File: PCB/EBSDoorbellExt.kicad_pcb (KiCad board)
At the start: 2 copper layers, 65.8 x 49 mm, 273 parts, among them P1 AC in, P2 Doorbell, Q1 BC846C, SW1 Power, SW2 FSM2JSMAA, U1 LM7809CT, U2 LM555N, U3 LTV-817

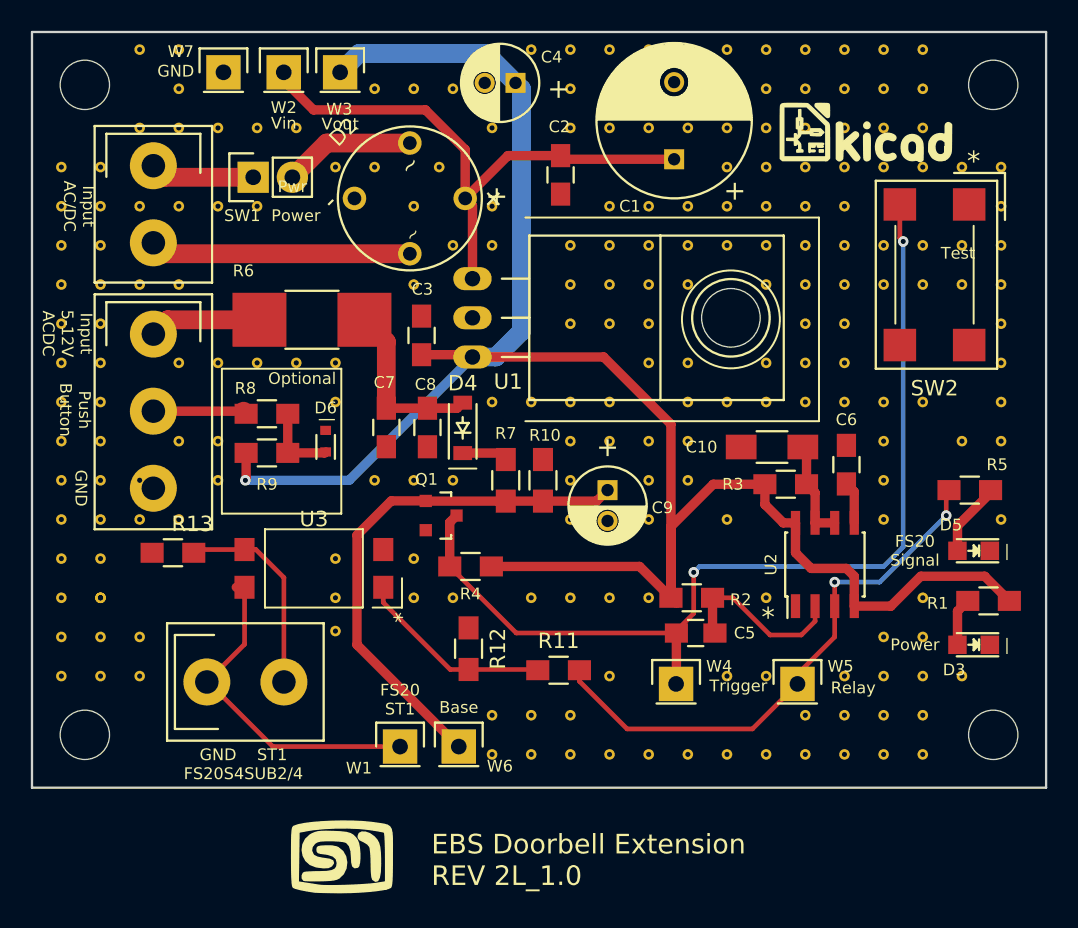
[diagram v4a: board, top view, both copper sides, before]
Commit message: Added protection diode on ground for voltage sensing
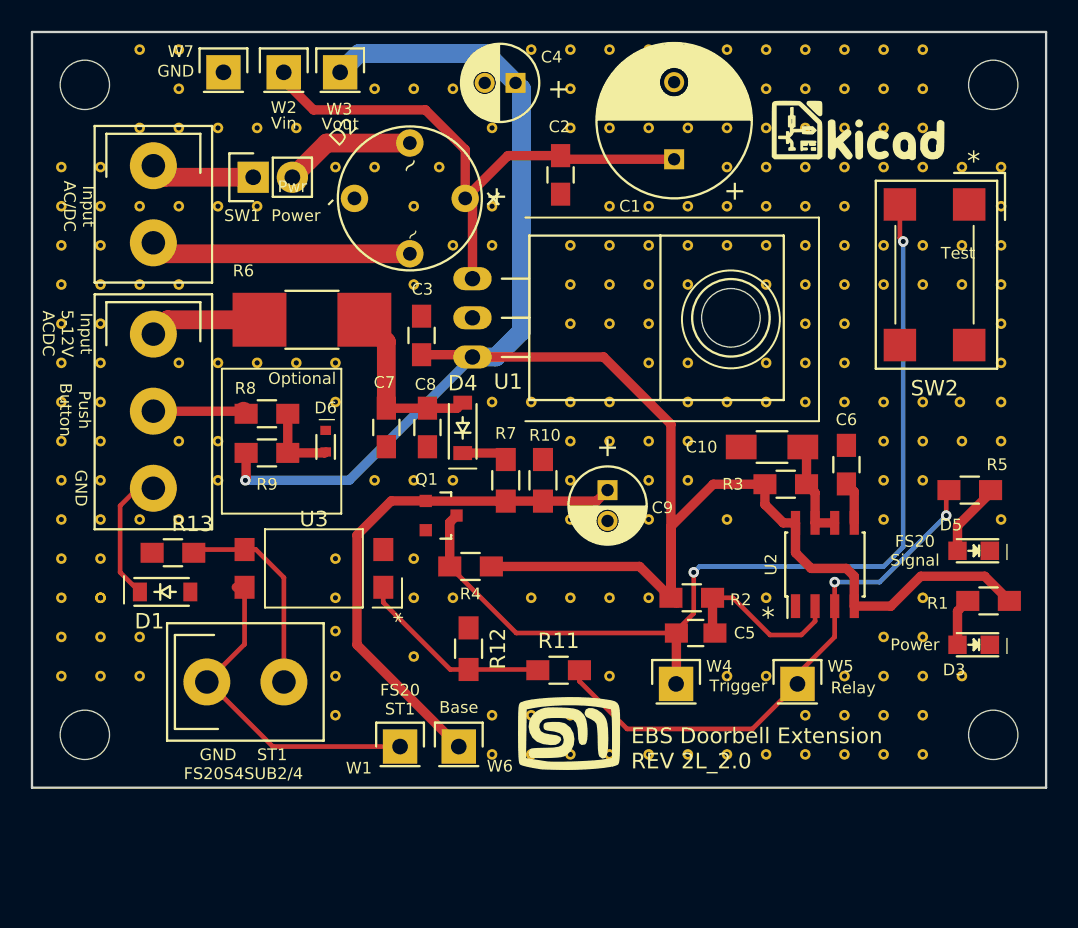
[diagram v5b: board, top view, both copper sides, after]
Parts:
- removed ST**312: Stitch_VIA, EBSDoorbellExt-Footprints:Stitch_VIA
- added D1: 1N4148W, Diodes_SMD:SOD-123, F.Cu at (138.8, 103.8)
- added ST**21712: Stitch_VIA, EBSDoorbellExt-Footprints:Stitch_VIA, F.Cu at (149.9, 111.8)
- added ST**21712: Stitch_VIA, EBSDoorbellExt-Footprints:Stitch_VIA, F.Cu at (154.9, 108.0)
- added ST**21712: Stitch_VIA, EBSDoorbellExt-Footprints:Stitch_VIA, F.Cu at (149.9, 109.2)
- added ST**2310: Stitch_VIA, EBSDoorbellExt-Footprints:Stitch_VIA, F.Cu at (190.4, 91.4)
- added ST**2310: Stitch_VIA, EBSDoorbellExt-Footprints:Stitch_VIA, F.Cu at (188.0, 96.5)
- added ST**2310: Stitch_VIA, EBSDoorbellExt-Footprints:Stitch_VIA, F.Cu at (188.0, 94.0)
- D2: footprint EBSDoorbellExt-Footprints:B80C1500G -> B80C1500G
- moved G*** 16.8 mm to (165.0, 112.9)
- moved G*** 0.52 mm to (183.8, 73.8)
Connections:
- P2 pad 3: GND -> Net-(D1-Pad1)
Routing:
- net Net-(D1-Pad1): track 0.00 -> 8.76 mm
- net Net-(C1-Pad1): track 37.5 -> 38.2 mm
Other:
- board text added: "EBS Doorbell Extension REV 2L_2.0"
- board text removed: "EBS Doorbell Extension REV 2L_1.0"

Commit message: Rev 2 gerbers and stensil order
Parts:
- removed ST**197: Stitch_VIA, EBSDoorbellExt-Footprints:Stitch_VIA
- added ST**21711: Stitch_VIA, EBSDoorbellExt-Footprints:Stitch_VIA, F.Cu at (142.2, 104.1)
- added ST**21711: Stitch_VIA, EBSDoorbellExt-Footprints:Stitch_VIA, F.Cu at (147.3, 104.1)
- added ST**21711: Stitch_VIA, EBSDoorbellExt-Footprints:Stitch_VIA, F.Cu at (147.3, 101.6)
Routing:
- net Net-(MOD1-Pad1): track 22.0 -> 21.4 mm
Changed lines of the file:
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@@
-(kicad_pcb (version 4) (host pcbnew 4.0.2-4+6225~38~ubuntu14.04.1-stable)
+(kicad_pcb (version 4) (host pcbnew 4.0.0-2.201512072331+6194~38~ubuntu14.04.1-stable)
   (general
-    (links 300)
+    (links 302)
     (no_connects 0)
     (area 126.257957 63.6926 199.878044 118.7834)
     (thickness 1.6)
     (drawings 38)
-    (tracks 157)
+    (tracks 156)
     (zones 0)
-    (modules 279)
+    (modules 281)
     (nets 26)
   )
@@
   )
   (setup
-    (last_trace_width 0.6096)
+    (last_trace_width 0.1524)
     (user_trace_width 0.3048)
     (user_trace_width 0.6096)
@@
     (add_net "Net-(SW2-Pad4)")
   )
+  (module EBSDoorbellExt-Footprints:Stitch_VIA (layer F.Cu)
+    (at 142.24 104.14)
+    (zone_connect 2)
+    (fp_text reference ST**21711 (at 0 3.556) (layer F.SilkS) hide
+      (effects (font (size 1 1) (thickness 0.15)))
+    )
+    (fp_text value Stitch_VIA (at 0 -3.81) (layer F.Fab) hide
+      (effects (font (size 1 1) (thickness 0.15)))
+    )
+    (pad 1 thru_hole circle (at 0 0) (size 0.6858 0.6858) (drill 0.3302) (layers *.Cu)
+      (net 2 GND) (zone_connect 2))
+  )
+  (module EBSDoorbellExt-Footprints:Stitch_VIA (layer F.Cu)
+    (at 147.32 104.14)
+    (zone_connect 2)
+    (fp_text reference ST**21711 (at 0 3.556) (layer F.SilkS) hide
+      (effects (font (size 1 1) (thickness 0.15)))
+    )
+    (fp_text value Stitch_VIA (at 0 -3.81) (layer F.Fab) hide
+      (effects (font (size 1 1) (thickness 0.15)))
+    )
+    (pad 1 thru_hole circle (at 0 0) (size 0.6858 0.6858) (drill 0.3302) (layers *.Cu)
+      (net 2 GND) (zone_connect 2))
+  )
+  (module EBSDoorbellExt-Footprints:Stitch_VIA (layer F.Cu)
+    (at 147.32 101.6)
+    (zone_connect 2)
+    (fp_text reference ST**21711 (at 0 3.556) (layer F.SilkS) hide
+      (effects (font (size 1 1) (thickness 0.15)))
+    )
+    (fp_text value Stitch_VIA (at 0 -3.81) (layer F.Fab) hide
+      (effects (font (size 1 1) (thickness 0.15)))
+    )
+    (pad 1 thru_hole circle (at 0 0) (size 0.6858 0.6858) (drill 0.3302) (layers *.Cu)
+      (net 2 GND) (zone_connect 2))
+  )
   (module B80C1500G (layer F.Cu)
     (at 154.686 78.232 225)
@@
   )
   (module EBSDoorbellExt-Footprints:Stitch_VIA (layer F.Cu)
-    (at 177.8 83.82)
-    (zone_connect 2)
-    (fp_text reference ST**197 (at 0 3.556) (layer F.SilkS) hide
-      (effects (font (size 1 1) (thickness 0.15)))
-    )
-    (fp_text value Stitch_VIA (at 0 -3.81) (layer F.Fab) hide
-      (effects (font (size 1 1) (thickness 0.15)))
-    )
-    (pad 1 thru_hole circle (at 0 0) (size 0.6858 0.6858) (drill 0.3302) (layers *.Cu)
-      (net 2 GND) (zone_connect 2))
-  )
-  (module EBSDoorbellExt-Footprints:Stitch_VIA (layer F.Cu)
     (at 172.72 83.82)
     (zone_connect 2)
@@
   (module EBSDoorbellExt-Footprints:LTV_817 (layer F.Cu)
     (at 148.463 102.235 90)
-    (fp_text reference U3 (at 3.2004 0 180) (layer F.SilkS)
+    (fp_text reference U3 (at -3.429 2.286 180) (layer F.SilkS)
       (effects (font (size 1 1) (thickness 0.15)))
     )
@@
     (effects (font (thickness 0.254)))
   )
-  (gr_text | (at 149.225 92.583 90) (layer F.SilkS)
+  (gr_text | (at 149.098 95.504 90) (layer F.SilkS)
     (effects (font (size 0.762 0.762) (thickness 0.1905)))
   )
@@
     (effects (font (size 0.762 0.762) (thickness 0.127)))
   )
-  (segment (start 158.75 83.439) (end 158.75 78.703898) (width 0.6096) (layer F.Cu) (net 1) (status C00000))
-  (segment (start 158.75 78.703898) (end 158.278102 78.232) (width 0.6096) (layer F.Cu) (net 1) (status C00000))
+  (segment (start 158.75 83.439) (end 158.75 78.703898) (width 0.6096) (layer F.Cu) (net 1))
+  (segment (start 158.75 78.703898) (end 158.278102 78.232) (width 0.6096) (layer F.Cu) (net 1))
   (segment (start 164.465 75.458) (end 164.699 75.692) (width 0.6096) (layer F.Cu) (net 1))
   (segment (start 164.699 75.692) (end 171.831 75.692) (width 0.6096) (layer F.Cu) (net 1))
@@
   (segment (start 143.963 103.46) (end 143.963 107.156) (width 0.3048) (layer F.Cu) (net 16))
   (segment (start 143.963 107.156) (end 141.518 109.601) (width 0.3048) (layer F.Cu) (net 16))
-  (segment (start 143.963 103.46) (end 143.428 103.46) (width 0.6096) (layer F.Cu) (net 16))
   (segment (start 138.049 87.035) (end 138.978 86.106) (width 1.2192) (layer F.Cu) (net 17))
   (segment (start 138.978 86.106) (end 144.9324 86.106) (width 1.2192) (layer F.Cu) (net 17))
